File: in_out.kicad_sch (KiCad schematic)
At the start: 4 parts, among them J2 Micro_SD_Card_Det1, SW1 SW_Push, SW2 SW_Push, U5 DM-OLED096-636

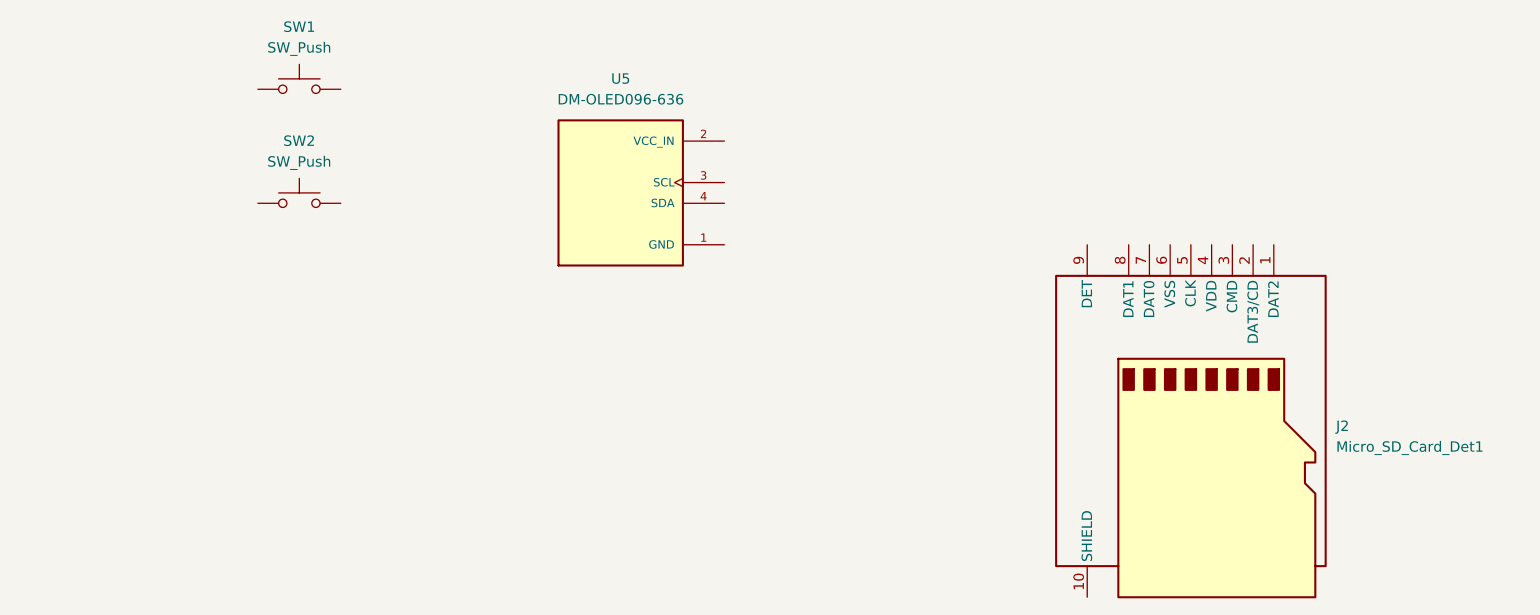
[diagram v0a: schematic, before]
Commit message: component placement inside schematic
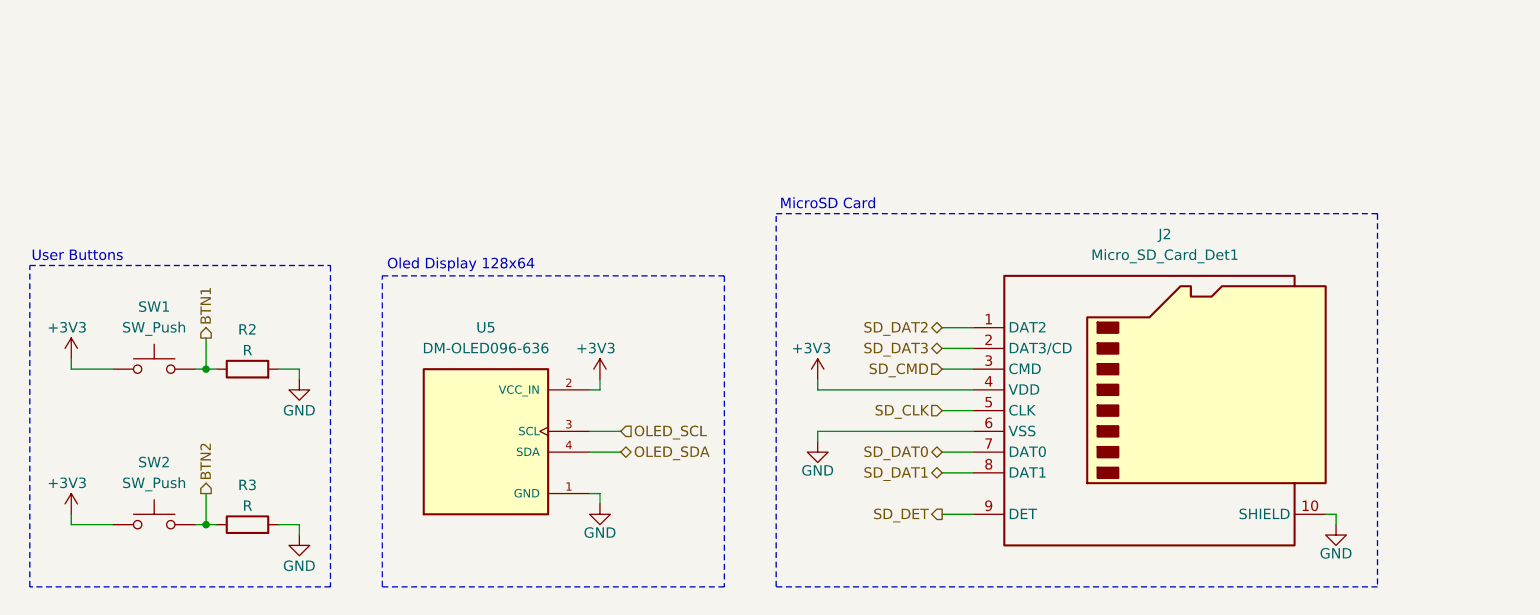
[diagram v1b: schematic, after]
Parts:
- added R2, R3: R, symbol Device:R
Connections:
- net GND: now reaches U5.1 (GND)
- net GND: now also J2.10 (SHIELD), J2.6 (VSS), R2.2, R3.2
- net +3V3: now reaches U5.2 (VCC_IN)
- net +3V3: now also J2.4 (VDD), SW1.1, SW2.1
- net OLED_SCL: now reaches U5.3 (SCL)
- net OLED_SDA: now reaches U5.4 (SDA)
- net BTN2: now reaches SW2.2
- net BTN2: now also R3.1
- net BTN1: now reaches SW1.2
- net BTN1: now also R2.1
- net SD_DAT2: now reaches J2.1 (DAT2)
- net SD_DAT3: now reaches J2.2 (DAT3/CD)
- net SD_CMD: now reaches J2.3 (CMD)
- net SD_CLK: now reaches J2.5 (CLK)
- net SD_DAT0: now reaches J2.7 (DAT0)
- net SD_DAT1: now reaches J2.8 (DAT1)
- net SD_DET: now reaches J2.9 (DET)
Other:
- note added: "MicroSD Card"
- note added: "Oled Display 128x64"
- note added: "User Buttons"
- moved on the sheet: J2, SW1, SW2, U5

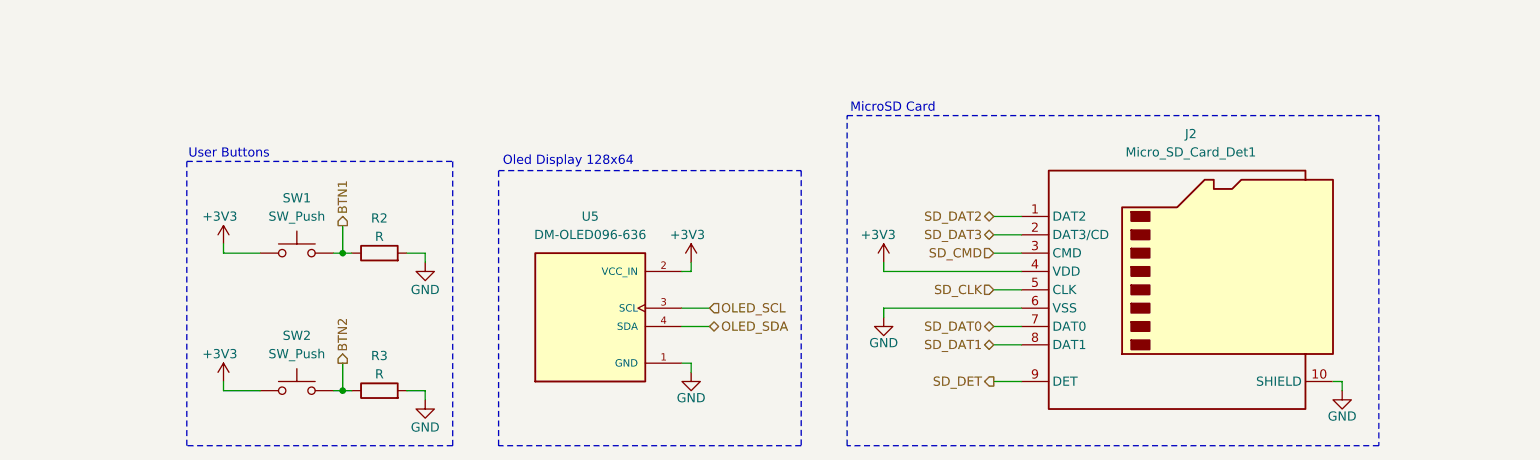
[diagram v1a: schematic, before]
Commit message: add RGB led
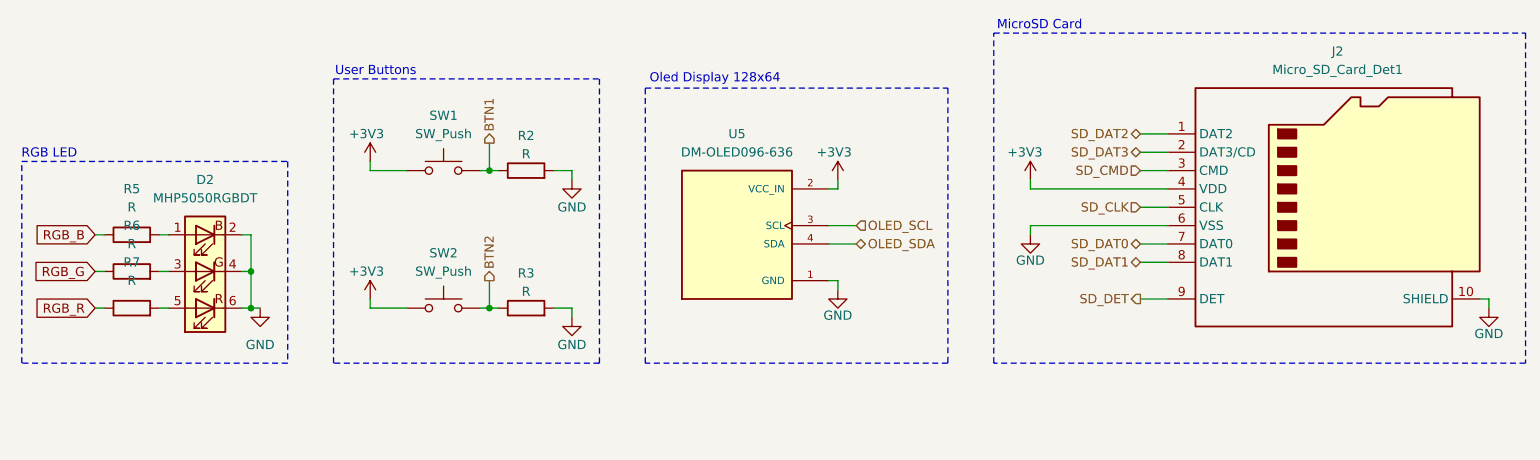
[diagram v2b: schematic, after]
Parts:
- added D2: MHP5050RGBDT, LED_SMD:LED_RGB_5050-6, symbol Device:LED_RGB
- added R5, R6, R7: R, symbol Device:R
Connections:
- net GND: now also D2.2 (BK), D2.4 (GK), D2.6 (RK)
- new net: D2.3 (GA), R6.2
- new net: D2.1 (BA), R5.2
- new net: D2.5 (RA), R7.2
- new net RGB_B: R5.1
- new net RGB_G: R6.1
- new net RGB_R: R7.1
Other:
- note added: "RGB LED"
- moved on the sheet: J2, R2, R3, SW1, SW2, U5

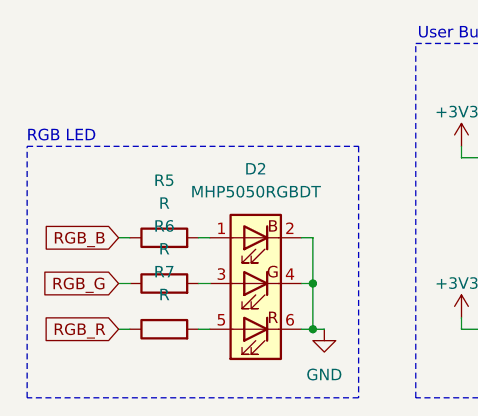
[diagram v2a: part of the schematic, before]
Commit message: fix rgb led labels
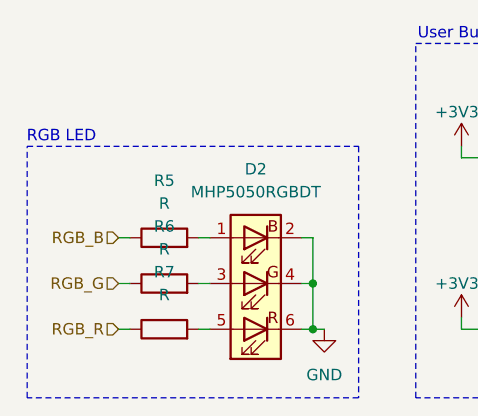
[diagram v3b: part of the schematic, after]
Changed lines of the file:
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@@
-		)
-	)
-	(global_label "RGB_B"
-		(shape input)
-		(at 52.07 91.44 180)
-		(fields_autoplaced yes)
-		(effects
-			(font
-				(size 1.27 1.27)
-			)
-			(justify right)
-		)
-		(property "Intersheetrefs" "${INTERSHEET_REFS}"
-			(at 43.0372 91.44 0)
-			(effects
-				(font
-					(size 1.27 1.27)
-				)
-				(justify right)
-				(hide yes)
-			)
-		)
-	)
-	(global_label "RGB_G"
-		(shape input)
-		(at 52.07 96.52 180)
-		(fields_autoplaced yes)
-		(effects
-			(font
-				(size 1.27 1.27)
-			)
-			(justify right)
-		)
-		(property "Intersheetrefs" "${INTERSHEET_REFS}"
-			(at 43.0372 96.52 0)
-			(effects
-				(font
-					(size 1.27 1.27)
-				)
-				(justify right)
-				(hide yes)
-			)
-		)
-	)
-	(global_label "RGB_R"
-		(shape input)
-		(at 52.07 101.6 180)
-		(fields_autoplaced yes)
-		(effects
-			(font
-				(size 1.27 1.27)
-			)
-			(justify right)
-		)
-		(property "Intersheetrefs" "${INTERSHEET_REFS}"
-			(at 43.0372 101.6 0)
-			(effects
-				(font
-					(size 1.27 1.27)
-				)
-				(justify right)
-				(hide yes)
-			)
 		)
 	)
@@
 		(shape bidirectional)
 		(at 196.85 80.01 180)
+		(effects
+			(font
+				(size 1.27 1.27)
+			)
+			(justify right)
+		)
+	)
+	(hierarchical_label "RGB_R"
+		(shape input)
+		(at 52.07 101.6 180)
+		(effects
+			(font
+				(size 1.27 1.27)
+			)
+			(justify right)
+		)
+	)
+	(hierarchical_label "RGB_G"
+		(shape input)
+		(at 52.07 96.52 180)
 		(effects
 			(font
@@
 		)
 	)
+	(hierarchical_label "RGB_B"
+		(shape input)
+		(at 52.07 91.44 180)
+		(effects
+			(font
+				(size 1.27 1.27)
+			)
+			(justify right)
+		)
+	)

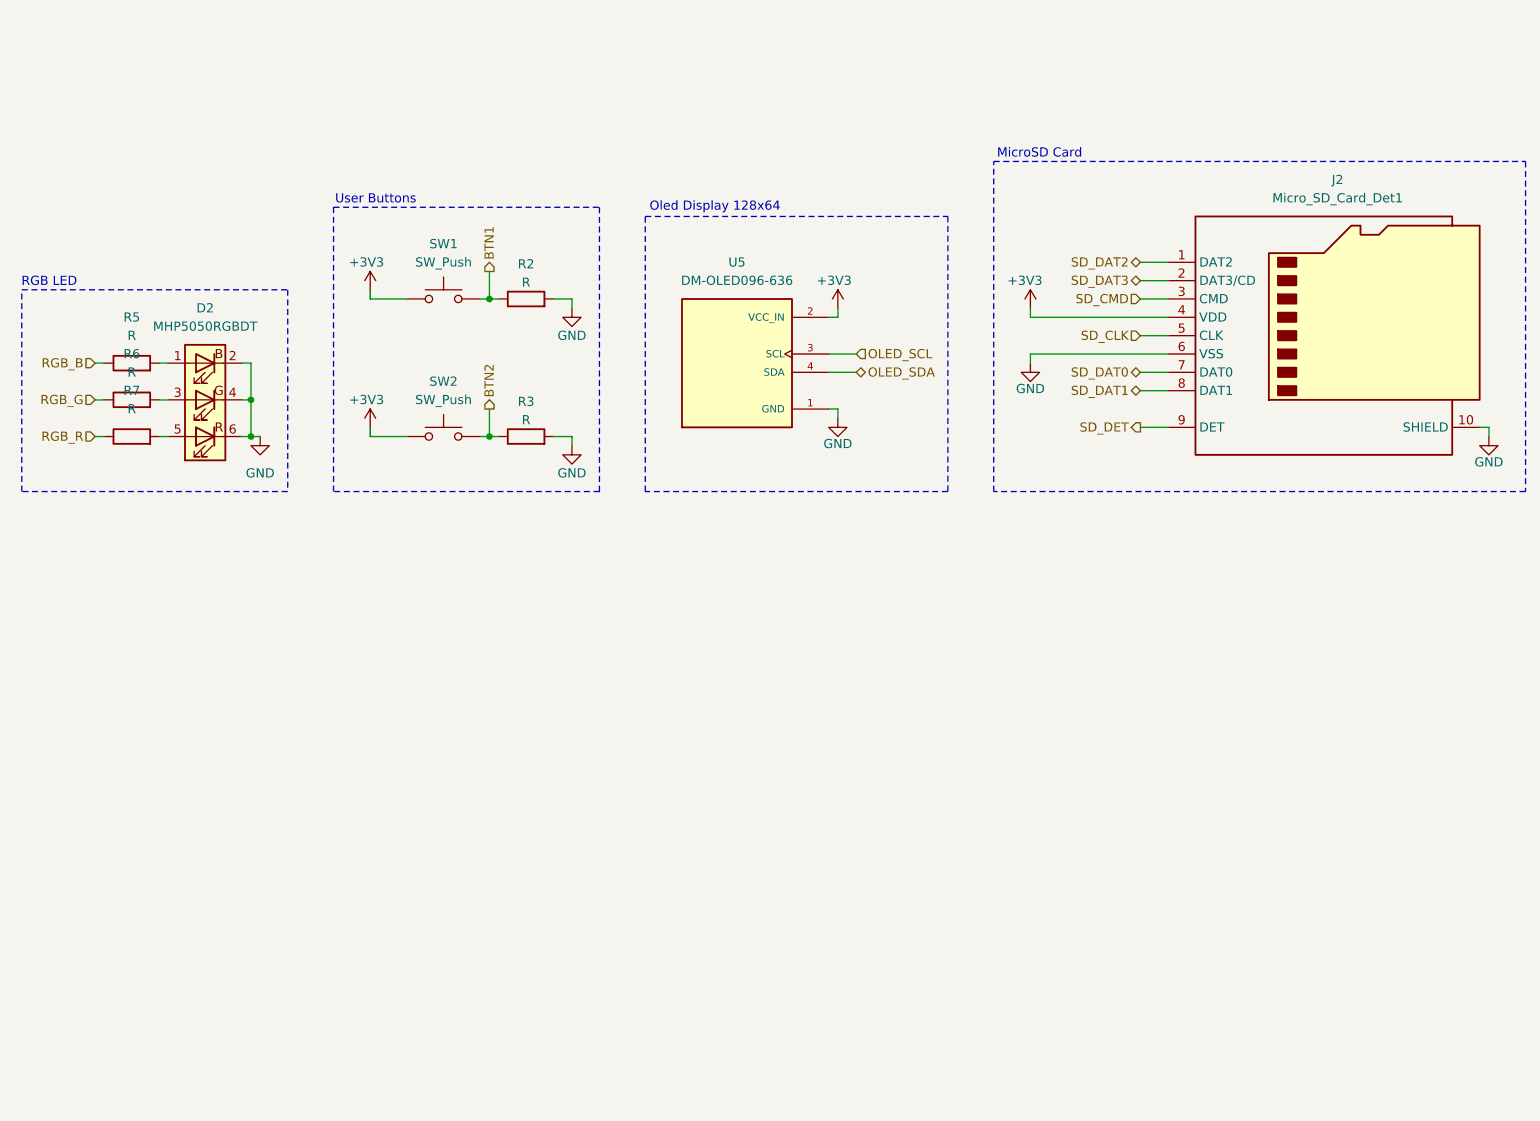
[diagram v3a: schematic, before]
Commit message: add external gpio connector
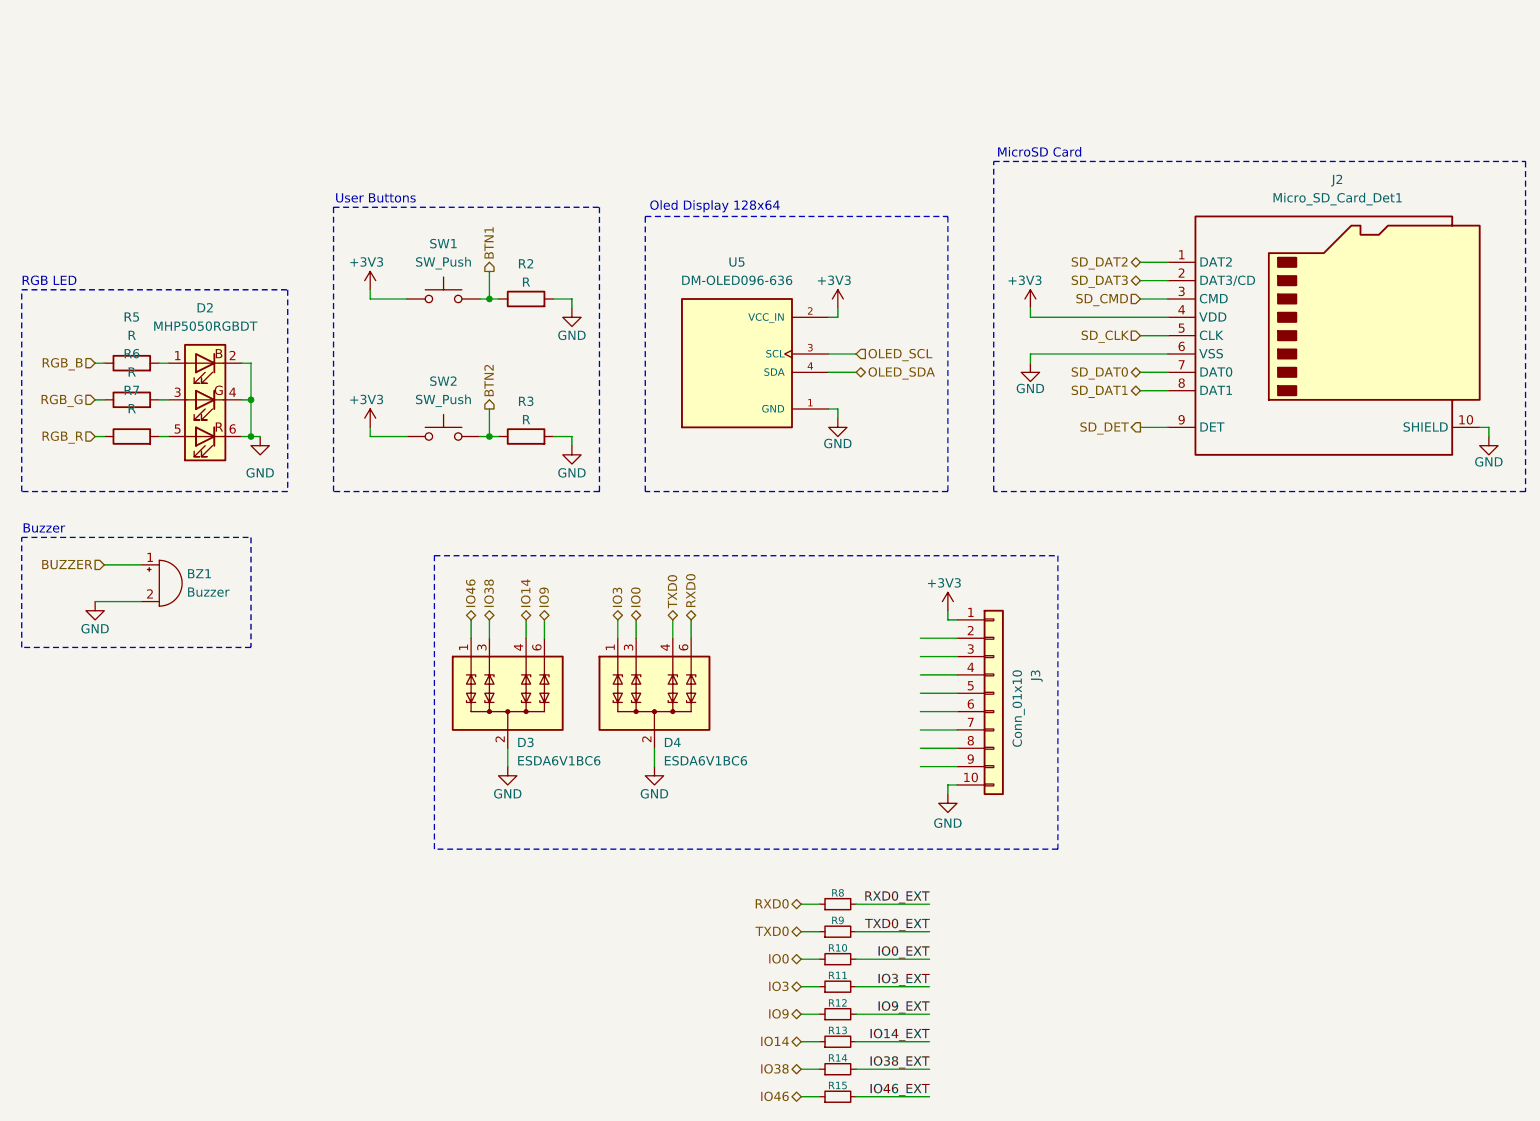
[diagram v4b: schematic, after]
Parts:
- added BZ1: Buzzer, symbol Device:Buzzer
- added D3, D4: ESDA6V1BC6, Package_TO_SOT_SMD:SOT-23-6, symbol Power_Protection:ESDA6V1BC6
- added J3: Conn_01x10, symbol Connector_Generic:Conn_01x10
- added R10, R11, R12, R13, R14, R15, R8, R9: R_Small, symbol Device:R_Small
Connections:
- net +3V3: now also J3.1 (Pin_1)
- net GND: now also BZ1.2 (-), D3.2 (COM), D3.5 (COM), D4.2 (COM), D4.5 (COM), J3.10 (Pin_10)
- new net BUZZER: BZ1.1 (+)
- new net IO0: D4.3 (TVS2), R10.1
- new net IO0_EXT: R10.2
- new net IO14: D3.4 (TVS3), R13.1
- new net IO14_EXT: R13.2
- new net IO3: D4.1 (TVS1), R11.1
- new net IO38: D3.3 (TVS2), R14.1
- new net IO38_EXT: R14.2
- new net IO3_EXT: R11.2
- new net IO46: D3.1 (TVS1), R15.1
- new net IO46_EXT: R15.2
- new net IO9: D3.6 (TVS4), R12.1
- new net IO9_EXT: R12.2
- new net RXD0: D4.6 (TVS4), R8.1
- new net RXD0_EXT: R8.2
- new net TXD0: D4.4 (TVS3), R9.1
- new net TXD0_EXT: R9.2
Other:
- note added: "Buzzer"

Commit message: add usbc esd protections
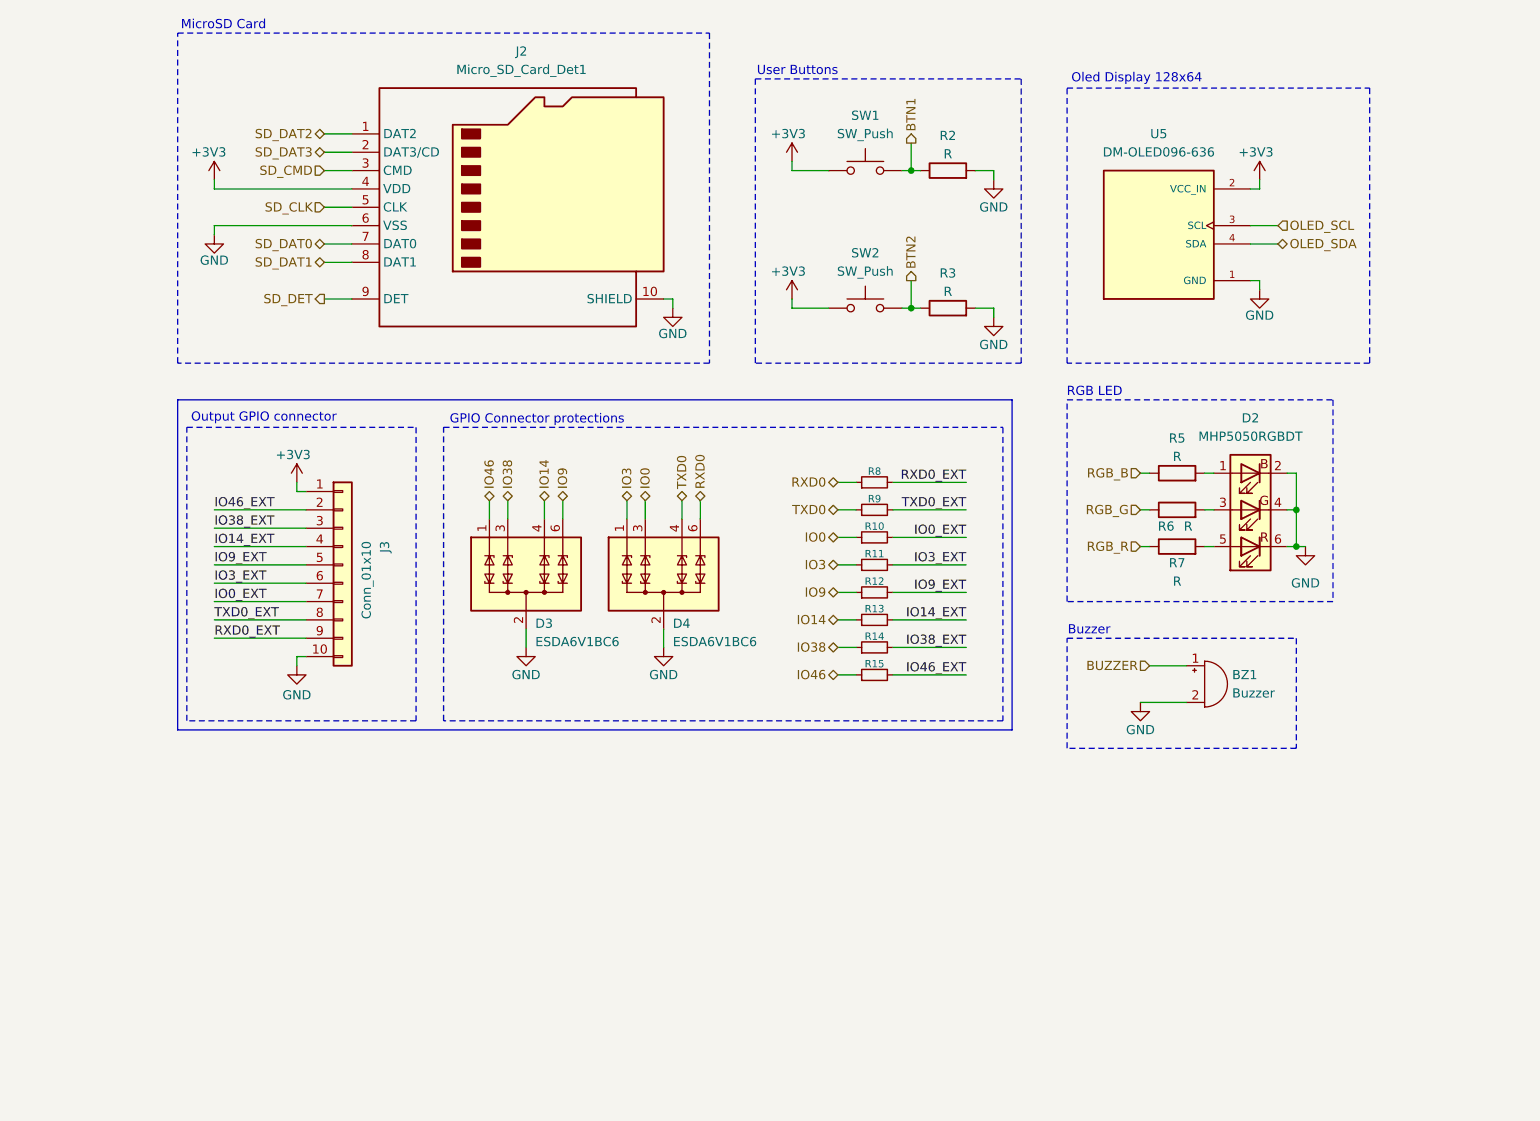
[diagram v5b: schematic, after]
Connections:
- net IO0_EXT: now also J3.7 (Pin_7)
- net IO14_EXT: now also J3.4 (Pin_4)
- net IO38_EXT: now also J3.3 (Pin_3)
- net IO3_EXT: now also J3.6 (Pin_6)
- net IO46_EXT: now also J3.2 (Pin_2)
- net IO9_EXT: now also J3.5 (Pin_5)
- net RXD0_EXT: now also J3.9 (Pin_9)
- net TXD0_EXT: now also J3.8 (Pin_8)
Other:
- note added: "GPIO Connector protections"
- note added: "Output GPIO connector"
- moved on the sheet: BZ1, D2, D3, D4, J2, J3, R10, R11, R12, R13, R14, R15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
